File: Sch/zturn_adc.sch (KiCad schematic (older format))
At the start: 1 part, among them IC1 CYUSB3014

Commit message: modify
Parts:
- removed unit 5 of IC1
- added TP1, TP2, TP3, TP4: TEST, symbol TEST
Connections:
- net labels added: FX3_GPIO[45], SPI_MISO, SPI_MOSI, SPI_SCK, SPI_SSN
- wire segments 0 -> 4
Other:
- moved on the sheet: IC1G
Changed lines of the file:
@@
 $EndDescr
 $Sheet
-S 1250 1200 1850 900
+S 1750 1650 1850 900
 U 589ADF9D
 F0 "FX3_clk_reset_cn" 60
@@
 $Comp
 L CYUSB3014 IC1
-U 5 1 58A0A752
-P 2850 3900
-F 0 "IC1" H 2850 1550 50  0000 C CNN
-F 1 "CYUSB3014" H 2850 6450 50  0000 C CNN
-F 2 "MODULE" H 2800 6200 50  0001 C CNN
-F 3 "DOCUMENTATION" H 2850 6350 50  0001 C CNN
-	5    2850 3900
-	1    0    0    -1
-$EndComp
-$Comp
-L CYUSB3014 IC1
 U 7 1 58A0A799
-P 4700 4650
-F 0 "IC1" H 4700 2300 50  0000 C CNN
-F 1 "CYUSB3014" H 4700 7200 50  0000 C CNN
-F 2 "MODULE" H 4650 6950 50  0001 C CNN
-F 3 "DOCUMENTATION" H 4700 7100 50  0001 C CNN
-	7    4700 4650
+P 6100 4750
+F 0 "IC1" H 6100 2400 50  0000 C CNN
+F 1 "CYUSB3014" H 6100 7300 50  0000 C CNN
+F 2 "MODULE" H 6050 7050 50  0001 C CNN
+F 3 "DOCUMENTATION" H 6100 7200 50  0001 C CNN
+	7    6100 4750
 	1    0    0    -1
 $EndComp
 $Sheet
-S 1300 2400 1700 650
+S 1800 2850 1700 650
 U 58A06B55
 F0 "FX3_power" 60
@@
 $EndSheet
 $Sheet
-S 7300 3600 1900 900
+S 7800 3350 1900 900
 U 58A1C0F3
 F0 "RF_in" 60
 F1 "RF_in.sch" 60
 $EndSheet
+Text Label 4950 4400 0    60   ~ 0
+SPI_SCK
+Text Label 4950 4300 0    60   ~ 0
+SPI_SSN
+Text Label 4950 4200 0    60   ~ 0
+SPI_MISO
+Text Label 4950 4100 0    60   ~ 0
+SPI_MOSI
+Wire Wire Line
+	5350 4400 4900 4400
+Wire Wire Line
+	5350 4300 4900 4300
+Wire Wire Line
+	5350 4200 4900 4200
+Wire Wire Line
+	5350 4100 4900 4100
+$Comp
+L TEST TP1
+U 1 1 58A3C918
+P 5350 4000
+F 0 "TP1" H 5350 4300 50  0000 C BNN
+F 1 "TEST" V 5350 4250 50  0000 C CNN
+F 2 "" H 5350 4000 50  0000 C CNN
+F 3 "" H 5350 4000 50  0000 C CNN
+	1    5350 4000
+	0    -1   -1   0
+$EndComp
+$Comp
+L TEST TP2
+U 1 1 58A3CCBA
+P 5350 4500
+F 0 "TP2" H 5350 4800 50  0000 C BNN
+F 1 "TEST" V 5350 4750 50  0000 C CNN
+F 2 "" H 5350 4500 50  0000 C CNN
+F 3 "" H 5350 4500 50  0000 C CNN
+	1    5350 4500
+	0    -1   -1   0
+$EndComp
+$Comp
+L TEST TP3
+U 1 1 58A3CCE7
+P 5350 4600
+F 0 "TP3" H 5350 4900 50  0000 C BNN
+F 1 "TEST" V 5350 4850 50  0000 C CNN
+F 2 "" H 5350 4600 50  0000 C CNN
+F 3 "" H 5350 4600 50  0000 C CNN
+	1    5350 4600
+	0    -1   -1   0
+$EndComp
+$Comp
+L TEST TP4
+U 1 1 58A3CFDC
+P 5350 4700
+F 0 "TP4" H 5350 5000 50  0000 C BNN
+F 1 "TEST" V 5350 4950 50  0000 C CNN
+F 2 "" H 5350 4700 50  0000 C CNN
+F 3 "" H 5350 4700 50  0000 C CNN
+	1    5350 4700
+	0    -1   -1   0
+$EndComp
+Text GLabel 5350 4900 0    60   Input ~ 0
+FX3_GPIO[45]
 $EndSCHEMATC

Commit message: update
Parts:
- removed IC1: CYUSB3014, MODULE, symbol CYUSB3014
- removed TP1, TP2, TP3, TP4: TEST, symbol TEST
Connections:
- net labels removed: FX3_GPIO[45], SPI_MISO, SPI_MOSI, SPI_SCK, SPI_SSN
- wire segments 4 -> 0
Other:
- note added: "OK"
- note added: "TODO: ADC Clock"
- note added: "TODO: Generate 1.2V"
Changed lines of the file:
@@
 $Descr A4 11693 8268
 encoding utf-8
-Sheet 1 5
+Sheet 1 6
 Title ""
 Date ""
@@
 F1 "FX3_clk_reset_cn.sch" 60
 $EndSheet
-$Comp
-L CYUSB3014 IC1
-U 7 1 58A0A799
-P 6100 4750
-F 0 "IC1" H 6100 2400 50  0000 C CNN
-F 1 "CYUSB3014" H 6100 7300 50  0000 C CNN
-F 2 "MODULE" H 6050 7050 50  0001 C CNN
-F 3 "DOCUMENTATION" H 6100 7200 50  0001 C CNN
-	7    6100 4750
-	1    0    0    -1
-$EndComp
 $Sheet
-S 1800 2850 1700 650
+S 1750 3150 1700 650
 U 58A06B55
 F0 "FX3_power" 60
@@
 $EndSheet
 $Sheet
-S 7800 1650 2450 1200
+S 4050 1650 2450 1200
 U 58A0A991
 F0 "FX3_DQ" 60
@@
 $EndSheet
 $Sheet
-S 7800 3350 1900 900
+S 4050 3150 1900 900
 U 58A1C0F3
 F0 "RF_in" 60
 F1 "RF_in.sch" 60
 $EndSheet
-Text Label 4950 4400 0    60   ~ 0
-SPI_SCK
-Text Label 4950 4300 0    60   ~ 0
-SPI_SSN
-Text Label 4950 4200 0    60   ~ 0
-SPI_MISO
-Text Label 4950 4100 0    60   ~ 0
-SPI_MOSI
-Wire Wire Line
-	5350 4400 4900 4400
-Wire Wire Line
-	5350 4300 4900 4300
-Wire Wire Line
-	5350 4200 4900 4200
-Wire Wire Line
-	5350 4100 4900 4100
-$Comp
-L TEST TP1
-U 1 1 58A3C918
-P 5350 4000
-F 0 "TP1" H 5350 4300 50  0000 C BNN
-F 1 "TEST" V 5350 4250 50  0000 C CNN
-F 2 "" H 5350 4000 50  0000 C CNN
-F 3 "" H 5350 4000 50  0000 C CNN
-	1    5350 4000
-	0    -1   -1   0
-$EndComp
-$Comp
-L TEST TP2
-U 1 1 58A3CCBA
-P 5350 4500
-F 0 "TP2" H 5350 4800 50  0000 C BNN
-F 1 "TEST" V 5350 4750 50  0000 C CNN
-F 2 "" H 5350 4500 50  0000 C CNN
-F 3 "" H 5350 4500 50  0000 C CNN
-	1    5350 4500
-	0    -1   -1   0
-$EndComp
-$Comp
-L TEST TP3
-U 1 1 58A3CCE7
-P 5350 4600
-F 0 "TP3" H 5350 4900 50  0000 C BNN
-F 1 "TEST" V 5350 4850 50  0000 C CNN
-F 2 "" H 5350 4600 50  0000 C CNN
-F 3 "" H 5350 4600 50  0000 C CNN
-	1    5350 4600
-	0    -1   -1   0
-$EndComp
-$Comp
-L TEST TP4
-U 1 1 58A3CFDC
-P 5350 4700
-F 0 "TP4" H 5350 5000 50  0000 C BNN
-F 1 "TEST" V 5350 4950 50  0000 C CNN
-F 2 "" H 5350 4700 50  0000 C CNN
-F 3 "" H 5350 4700 50  0000 C CNN
-	1    5350 4700
-	0    -1   -1   0
-$EndComp
-Text GLabel 5350 4900 0    60   Input ~ 0
-FX3_GPIO[45]
+$Sheet
+S 1750 4450 1400 850
+U 58A517F2
+F0 "FX3_GPIO" 60
+F1 "FX3_GPIO.sch" 60
+$EndSheet
+Text Notes 1500 5000 0    60   ~ 0
+OK
+Text Notes 1400 2100 0    60   ~ 0
+OK
+Text Notes 700  3600 0    60   ~ 0
+TODO: Generate 1.2V
+Text Notes 6700 2350 0    60   ~ 0
+TODO: ADC Clock
 $EndSCHEMATC

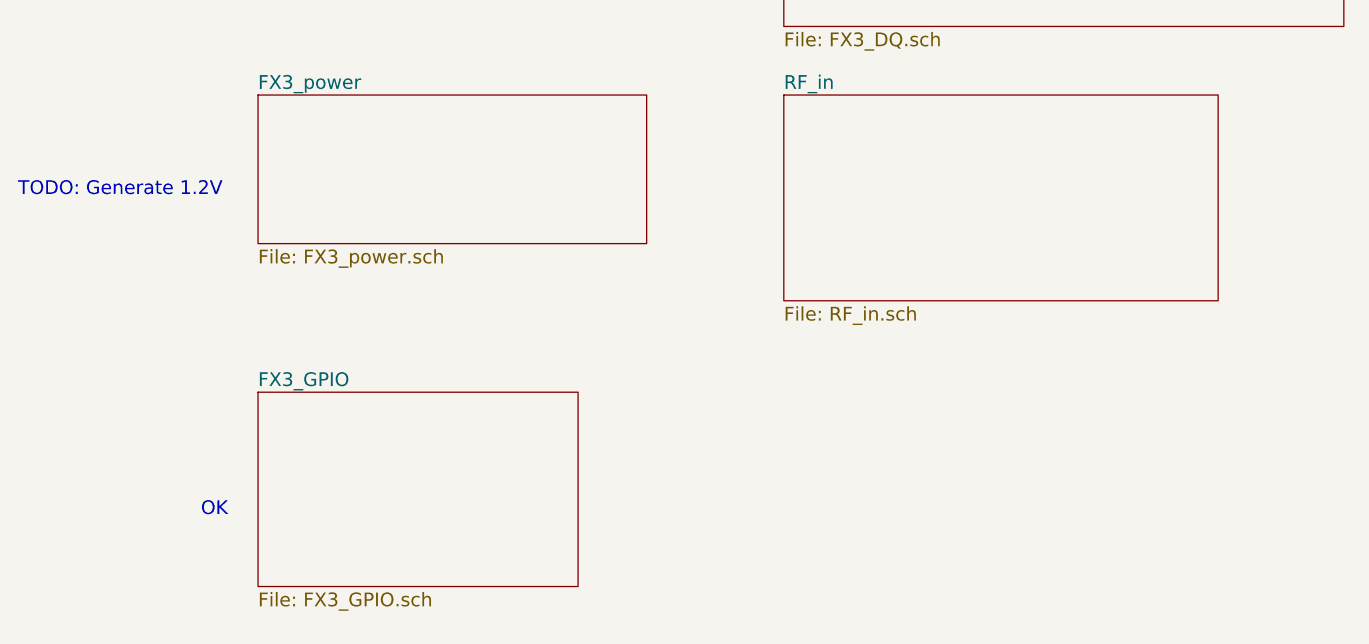
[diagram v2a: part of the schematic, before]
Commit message: Add 1.2V
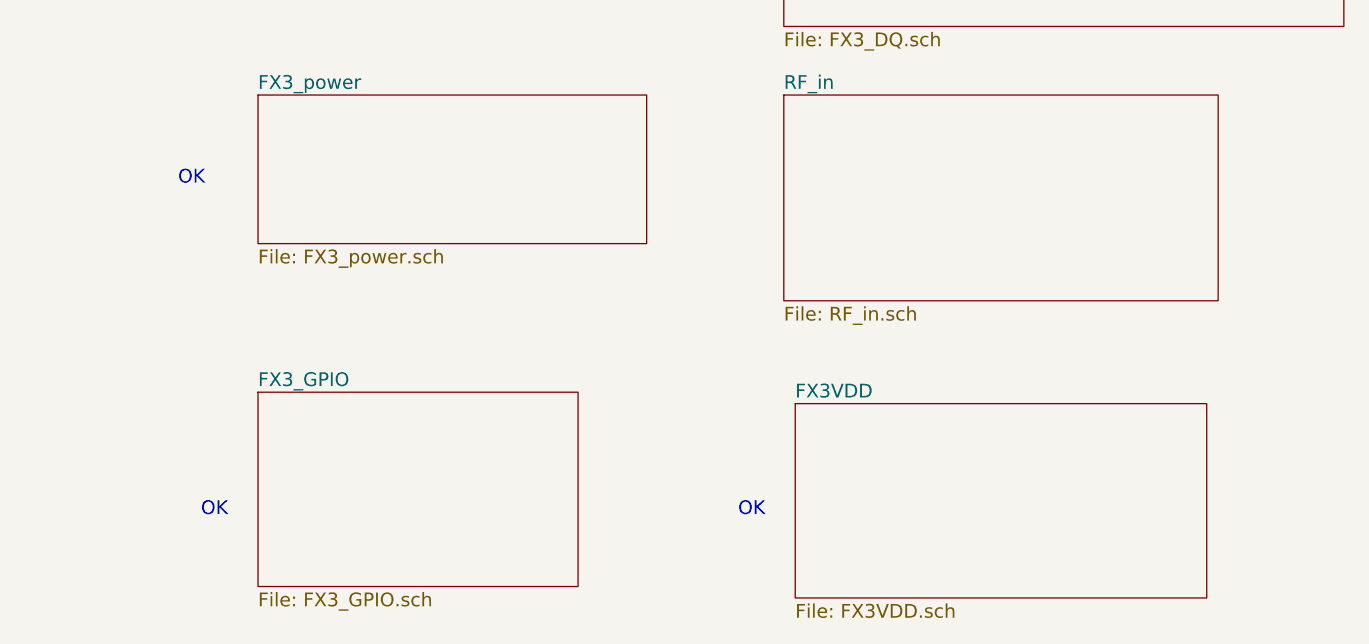
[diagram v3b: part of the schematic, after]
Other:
- note removed: "TODO: Generate 1.2V"
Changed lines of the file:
@@
 $Descr A4 11693 8268
 encoding utf-8
-Sheet 1 6
+Sheet 1 7
 Title ""
 Date ""
@@
 Text Notes 1400 2100 0    60   ~ 0
 OK
-Text Notes 700  3600 0    60   ~ 0
-TODO: Generate 1.2V
 Text Notes 6700 2350 0    60   ~ 0
 TODO: ADC Clock
+$Sheet
+S 4100 4500 1800 850
+U 58A458E3
+F0 "FX3VDD" 60
+F1 "FX3VDD.sch" 60
+$EndSheet
+Text Notes 3850 5000 0    60   ~ 0
+OK
+Text Notes 1400 3550 0    60   ~ 0
+OK
 $EndSCHEMATC
